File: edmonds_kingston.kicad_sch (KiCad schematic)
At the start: 22 parts

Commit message: single ferry track checkpoint
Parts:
- removed LED1015, LED1016, LED1017, LED1018, LED1019, LED1020, LED1021, LED1022, LED1023, LED1024: WS2812B-2020, EasyEDA:LED-SMD_4P-L2.0-W2.0-TL_WS2812B-2020, symbol EasyEDA:WS2812B-2020

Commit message: checkpoint before label plugin
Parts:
- added LED1011, LED1012, LED1013, LED1014: WS2812B-2020, EasyEDA:LED-SMD_4P-L2.0-W2.0-TL_WS2812B-2020, symbol EasyEDA:WS2812B-2020
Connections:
- net +VLED: now also LED1011.4 (VDD), LED1012.4 (VDD), LED1013.4 (VDD), LED1014.4 (VDD)
- net GND: now also LED1011.2 (GND), LED1012.2 (GND), LED1013.2 (GND), LED1014.2 (GND)
- net at LED1010.1 (DO): now also LED1011.3 (DI)
- new net: LED1013.1 (DO), LED1014.3 (DI)
- new net: LED1012.1 (DO), LED1013.3 (DI)
- new net: LED1011.1 (DO), LED1012.3 (DI)

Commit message: Add rail labels
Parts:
- renumbered LED447 to LED1001, LED1001 to LED1002, LED1002 to LED1003, LED1003 to LED1004, LED1004 to LED1005, LED1005 to LED1006, LED1006 to LED1007, LED1007 to LED1008, LED1008 to LED1009, LED1009 to LED1010, LED1010 to LED1011, LED1011 to LED1012, LED1012 to LED1013, LED1013 to LED1014, LED1014 to LED1015
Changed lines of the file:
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@@
 		(dnp no)
 		(fields_autoplaced yes)
-		(property "Reference" "LED1003"
+		(property "Reference" "LED1004"
 			(at 93.98 26.67 0)
 			(show_name no)
@@
 			(project "transit"
 				(path "/3763eade-a8c8-4ec0-9cf2-9db4442b4ee5/153adc6e-a3b0-4527-a19a-87e28aab4b4d/8f5c64ad-8b76-4e92-82ed-624af7bc34b2"
-					(reference "LED1003")
+					(reference "LED1004")
 					(unit 1)
 				)
@@
 		(dnp no)
 		(fields_autoplaced yes)
-		(property "Reference" "LED1013"
+		(property "Reference" "LED1014"
 			(at 185.42 46.99 0)
 			(show_name no)
@@
 			(project "transit"
 				(path "/3763eade-a8c8-4ec0-9cf2-9db4442b4ee5/153adc6e-a3b0-4527-a19a-87e28aab4b4d/8f5c64ad-8b76-4e92-82ed-624af7bc34b2"
-					(reference "LED1013")
+					(reference "LED1014")
 					(unit 1)
 				)
@@
 		(dnp no)
 		(fields_autoplaced yes)
-		(property "Reference" "LED1014"
+		(property "Reference" "LED1015"
 			(at 207.01 46.99 0)
 			(show_name no)
@@
 			(project "transit"
 				(path "/3763eade-a8c8-4ec0-9cf2-9db4442b4ee5/153adc6e-a3b0-4527-a19a-87e28aab4b4d/8f5c64ad-8b76-4e92-82ed-624af7bc34b2"
-					(reference "LED1014")
+					(reference "LED1015")
 					(unit 1)
 				)
@@
 		(dnp no)
 		(fields_autoplaced yes)
-		(property "Reference" "LED1008"
+		(property "Reference" "LED1009"
 			(at 83.82 46.99 0)
 			(show_name no)
@@
 			(project "transit"
 				(path "/3763eade-a8c8-4ec0-9cf2-9db4442b4ee5/153adc6e-a3b0-4527-a19a-87e28aab4b4d/8f5c64ad-8b76-4e92-82ed-624af7bc34b2"
-					(reference "LED1008")
+					(reference "LED1009")
 					(unit 1)
 				)
@@
 		(dnp no)
 		(fields_autoplaced yes)
-		(property "Reference" "LED1012"
+		(property "Reference" "LED1013"
 			(at 165.1 46.99 0)
 			(show_name no)
@@
 			(project "transit"
 				(path "/3763eade-a8c8-4ec0-9cf2-9db4442b4ee5/153adc6e-a3b0-4527-a19a-87e28aab4b4d/8f5c64ad-8b76-4e92-82ed-624af7bc34b2"
-					(reference "LED1012")
+					(reference "LED1013")
 					(unit 1)
 				)
@@
 		(dnp no)
 		(fields_autoplaced yes)
-		(property "Reference" "LED1001"
+		(property "Reference" "LED1002"
 			(at 53.34 26.67 0)
 			(show_name no)
@@
 			(project "transit"
 				(path "/3763eade-a8c8-4ec0-9cf2-9db4442b4ee5/153adc6e-a3b0-4527-a19a-87e28aab4b4d/8f5c64ad-8b76-4e92-82ed-624af7bc34b2"
-					(reference "LED1001")
+					(reference "LED1002")
 					(unit 1)
 				)
@@
 		(dnp no)
 		(fields_autoplaced yes)
-		(property "Reference" "LED1002"
+		(property "Reference" "LED1003"
 			(at 73.66 26.67 0)
 			(show_name no)
@@
 			(project "transit"
 				(path "/3763eade-a8c8-4ec0-9cf2-9db4442b4ee5/153adc6e-a3b0-4527-a19a-87e28aab4b4d/8f5c64ad-8b76-4e92-82ed-624af7bc34b2"
-					(reference "LED1002")
+					(reference "LED1003")
 					(unit 1)
 				)
@@
 		(dnp no)
 		(fields_autoplaced yes)
-		(property "Reference" "LED1011"
+		(property "Reference" "LED1012"
 			(at 144.78 46.99 0)
 			(show_name no)
@@
 			(project "transit"
 				(path "/3763eade-a8c8-4ec0-9cf2-9db4442b4ee5/153adc6e-a3b0-4527-a19a-87e28aab4b4d/8f5c64ad-8b76-4e92-82ed-624af7bc34b2"
-					(reference "LED1011")
+					(reference "LED1012")
 					(unit 1)
 				)
@@
 		(dnp no)
 		(fields_autoplaced yes)
-		(property "Reference" "LED1005"
+		(property "Reference" "LED1006"
 			(at 134.62 26.67 0)
 			(show_name no)
@@
 			(project "transit"
 				(path "/3763eade-a8c8-4ec0-9cf2-9db4442b4ee5/153adc6e-a3b0-4527-a19a-87e28aab4b4d/8f5c64ad-8b76-4e92-82ed-624af7bc34b2"
-					(reference "LED1005")
+					(reference "LED1006")
 					(unit 1)
 				)
@@
 		(dnp no)
 		(fields_autoplaced yes)
-		(property "Reference" "LED1009"
+		(property "Reference" "LED1010"
 			(at 104.14 46.99 0)
 			(show_name no)
@@
 			(project "transit"
 				(path "/3763eade-a8c8-4ec0-9cf2-9db4442b4ee5/153adc6e-a3b0-4527-a19a-87e28aab4b4d/8f5c64ad-8b76-4e92-82ed-624af7bc34b2"
-					(reference "LED1009")
+					(reference "LED1010")
 					(unit 1)
 				)
@@
 		(dnp no)
 		(fields_autoplaced yes)
-		(property "Reference" "LED1007"
+		(property "Reference" "LED1008"
 			(at 63.5 46.99 0)
 			(show_name no)
@@
 			(project "transit"
 				(path "/3763eade-a8c8-4ec0-9cf2-9db4442b4ee5/153adc6e-a3b0-4527-a19a-87e28aab4b4d/8f5c64ad-8b76-4e92-82ed-624af7bc34b2"
-					(reference "LED1007")
+					(reference "LED1008")
 					(unit 1)
 				)
@@
 		(dnp no)
 		(fields_autoplaced yes)
-		(property "Reference" "LED1004"
+		(property "Reference" "LED1005"
 			(at 114.3 26.67 0)
 			(show_name no)
@@
 			(project "transit"
 				(path "/3763eade-a8c8-4ec0-9cf2-9db4442b4ee5/153adc6e-a3b0-4527-a19a-87e28aab4b4d/8f5c64ad-8b76-4e92-82ed-624af7bc34b2"
-					(reference "LED1004")
+					(reference "LED1005")
 					(unit 1)
 				)
@@
 		(dnp no)
 		(fields_autoplaced yes)
-		(property "Reference" "LED1010"
+		(property "Reference" "LED1011"
 			(at 124.46 46.99 0)
 			(show_name no)
@@
 			(project "transit"
 				(path "/3763eade-a8c8-4ec0-9cf2-9db4442b4ee5/153adc6e-a3b0-4527-a19a-87e28aab4b4d/8f5c64ad-8b76-4e92-82ed-624af7bc34b2"
-					(reference "LED1010")
+					(reference "LED1011")
 					(unit 1)
 				)
@@
 		(dnp no)
 		(fields_autoplaced yes)
-		(property "Reference" "LED1006"
+		(property "Reference" "LED1007"
 			(at 154.94 26.67 0)
 			(show_name no)
@@
 			(project "transit"
 				(path "/3763eade-a8c8-4ec0-9cf2-9db4442b4ee5/153adc6e-a3b0-4527-a19a-87e28aab4b4d/8f5c64ad-8b76-4e92-82ed-624af7bc34b2"
-					(reference "LED1006")
+					(reference "LED1007")
 					(unit 1)
 				)
@@
 		(in_pos_files yes)
 		(dnp no)
-		(property "Reference" "LED447"
+		(property "Reference" "LED1001"
 			(at 31.75 26.67 0)
 			(show_name no)
@@
 			(project "transit"
 				(path "/3763eade-a8c8-4ec0-9cf2-9db4442b4ee5/153adc6e-a3b0-4527-a19a-87e28aab4b4d/8f5c64ad-8b76-4e92-82ed-624af7bc34b2"
-					(reference "LED447")
+					(reference "LED1001")
 					(unit 1)
 				)

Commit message: routing complete
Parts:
- removed C402: 150u, EasyEDA:CAP-SMD_L3.5-W2.8, symbol EasyEDA:CL21B106KOQNNNE
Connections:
- net +VLED: now also LED1003.4 (VDD)
- net at LED1004.1 (DO): now also LED1003.3 (DI); no longer LED1005.3 (DI)
- net at LED1003.1 (DO): now also LED1002.3 (DI); no longer LED1004.3 (DI)
- net at LED1014.1 (DO): now also LED1013.3 (DI); no longer LED1015.3 (DI)
- net at LED1013.1 (DO): now also LED1012.3 (DI); no longer LED1014.3 (DI)
- net at LED1015.1 (DO): now also LED1014.3 (DI)
- net at LED1010.3 (DI): now also LED1011.1 (DO); no longer LED1009.1 (DO)
- net at LED1009.3 (DI): now also LED1010.1 (DO); no longer LED1008.1 (DO)
- net at LED1012.1 (DO): now also LED1011.3 (DI); no longer LED1013.3 (DI)
- net at LED1002.1 (DO): now also LED1001.4 (DIN); no longer LED1003.3 (DI)
- net EDMONDS_MUKILTEO: now reaches LED1001.2 (DOUT)
- net EDMONDS_MUKILTEO: no longer LED1002.3 (DI)
- net at LED1007.3 (DI): now also LED1008.1 (DO); no longer LED1006.1 (DO)
- net at LED1005.1 (DO): now also LED1004.3 (DI); no longer LED1006.3 (DI)
- net at LED1008.3 (DI): now also LED1009.1 (DO); no longer LED1007.1 (DO)
- new net: LED1005.3 (DI), LED1006.1 (DO)
- new net: LED1006.3 (DI), LED1007.1 (DO)
- new net KINGSTON_EDMONDS: LED1015.3 (DI)
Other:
- moved on the sheet: LED1001

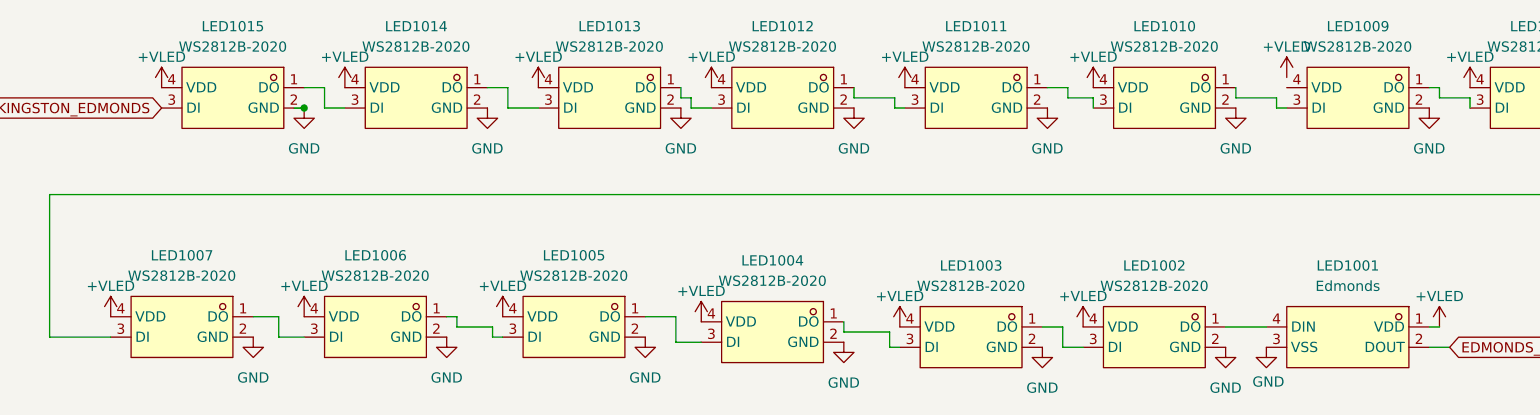
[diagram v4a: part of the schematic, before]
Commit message: reflow reference designators
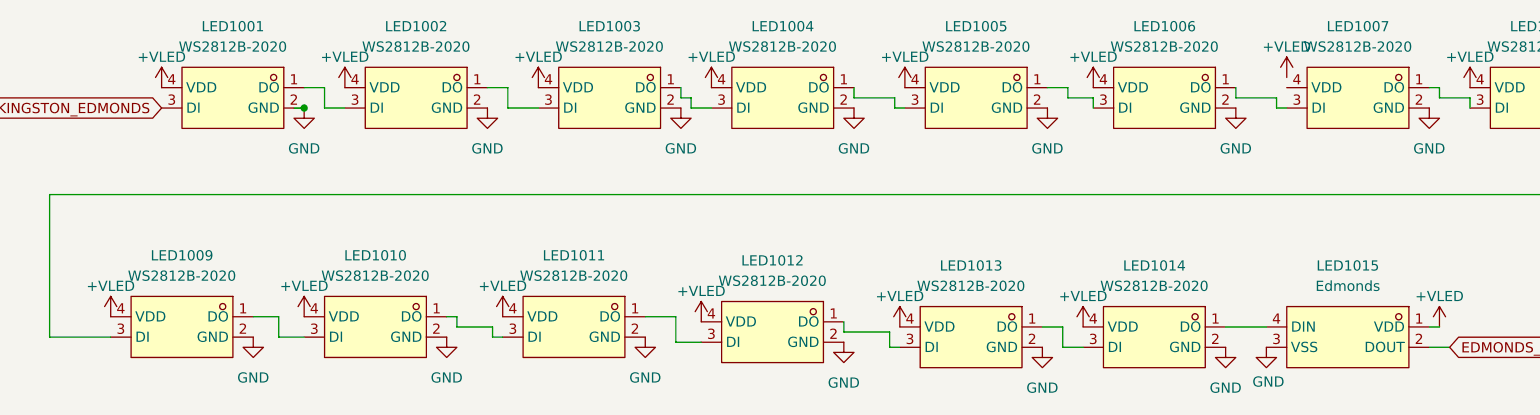
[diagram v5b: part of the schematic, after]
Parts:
- renumbered LED1015 to LED1001, LED1014 to LED1002, LED1013 to LED1003, LED1012 to LED1004, LED1011 to LED1005, LED1010 to LED1006, LED1009 to LED1007, LED1007 to LED1009, LED1006 to LED1010, LED1005 to LED1011, LED1004 to LED1012, LED1003 to LED1013, LED1002 to LED1014, LED1001 to LED1015
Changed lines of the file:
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@@
 		(dnp no)
 		(fields_autoplaced yes)
-		(property "Reference" "LED1002"
+		(property "Reference" "LED1014"
 			(at 171.45 64.135 0)
 			(show_name no)
@@
 			(project "transit"
 				(path "/3763eade-a8c8-4ec0-9cf2-9db4442b4ee5/153adc6e-a3b0-4527-a19a-87e28aab4b4d/8f5c64ad-8b76-4e92-82ed-624af7bc34b2"
-					(reference "LED1002")
+					(reference "LED1014")
 					(unit 1)
 				)
@@
 		(dnp no)
 		(fields_autoplaced yes)
-		(property "Reference" "LED1010"
+		(property "Reference" "LED1006"
 			(at 172.72 34.29 0)
 			(show_name no)
@@
 			(project "transit"
 				(path "/3763eade-a8c8-4ec0-9cf2-9db4442b4ee5/153adc6e-a3b0-4527-a19a-87e28aab4b4d/8f5c64ad-8b76-4e92-82ed-624af7bc34b2"
-					(reference "LED1010")
+					(reference "LED1006")
 					(unit 1)
 				)
@@
 		(dnp no)
 		(fields_autoplaced yes)
-		(property "Reference" "LED1011"
+		(property "Reference" "LED1005"
 			(at 149.225 34.29 0)
 			(show_name no)
@@
 			(project "transit"
 				(path "/3763eade-a8c8-4ec0-9cf2-9db4442b4ee5/153adc6e-a3b0-4527-a19a-87e28aab4b4d/8f5c64ad-8b76-4e92-82ed-624af7bc34b2"
-					(reference "LED1011")
+					(reference "LED1005")
 					(unit 1)
 				)
@@
 		(dnp no)
 		(fields_autoplaced yes)
-		(property "Reference" "LED1013"
+		(property "Reference" "LED1003"
 			(at 103.505 34.29 0)
 			(show_name no)
@@
 			(project "transit"
 				(path "/3763eade-a8c8-4ec0-9cf2-9db4442b4ee5/153adc6e-a3b0-4527-a19a-87e28aab4b4d/8f5c64ad-8b76-4e92-82ed-624af7bc34b2"
-					(reference "LED1013")
+					(reference "LED1003")
 					(unit 1)
 				)
@@
 		(dnp no)
 		(fields_autoplaced yes)
-		(property "Reference" "LED1009"
+		(property "Reference" "LED1007"
 			(at 196.85 34.29 0)
 			(show_name no)
@@
 			(project "transit"
 				(path "/3763eade-a8c8-4ec0-9cf2-9db4442b4ee5/153adc6e-a3b0-4527-a19a-87e28aab4b4d/8f5c64ad-8b76-4e92-82ed-624af7bc34b2"
-					(reference "LED1009")
+					(reference "LED1007")
 					(unit 1)
 				)
@@
 		(dnp no)
 		(fields_autoplaced yes)
-		(property "Reference" "LED1015"
+		(property "Reference" "LED1001"
 			(at 56.515 34.29 0)
 			(show_name no)
@@
 			(project "transit"
 				(path "/3763eade-a8c8-4ec0-9cf2-9db4442b4ee5/153adc6e-a3b0-4527-a19a-87e28aab4b4d/8f5c64ad-8b76-4e92-82ed-624af7bc34b2"
-					(reference "LED1015")
+					(reference "LED1001")
 					(unit 1)
 				)
@@
 		(dnp no)
 		(fields_autoplaced yes)
-		(property "Reference" "LED1012"
+		(property "Reference" "LED1004"
 			(at 125.095 34.29 0)
 			(show_name no)
@@
 			(project "transit"
 				(path "/3763eade-a8c8-4ec0-9cf2-9db4442b4ee5/153adc6e-a3b0-4527-a19a-87e28aab4b4d/8f5c64ad-8b76-4e92-82ed-624af7bc34b2"
-					(reference "LED1012")
+					(reference "LED1004")
 					(unit 1)
 				)
@@
 		(dnp no)
 		(fields_autoplaced yes)
-		(property "Reference" "LED1003"
+		(property "Reference" "LED1013"
 			(at 148.59 64.135 0)
 			(show_name no)
@@
 			(project "transit"
 				(path "/3763eade-a8c8-4ec0-9cf2-9db4442b4ee5/153adc6e-a3b0-4527-a19a-87e28aab4b4d/8f5c64ad-8b76-4e92-82ed-624af7bc34b2"
-					(reference "LED1003")
+					(reference "LED1013")
 					(unit 1)
 				)
@@
 		(dnp no)
 		(fields_autoplaced yes)
-		(property "Reference" "LED1014"
+		(property "Reference" "LED1002"
 			(at 79.375 34.29 0)
 			(show_name no)
@@
 			(project "transit"
 				(path "/3763eade-a8c8-4ec0-9cf2-9db4442b4ee5/153adc6e-a3b0-4527-a19a-87e28aab4b4d/8f5c64ad-8b76-4e92-82ed-624af7bc34b2"
-					(reference "LED1014")
+					(reference "LED1002")
 					(unit 1)
 				)
@@
 		(dnp no)
 		(fields_autoplaced yes)
-		(property "Reference" "LED1005"
+		(property "Reference" "LED1011"
 			(at 99.06 62.865 0)
 			(show_name no)
@@
 			(project "transit"
 				(path "/3763eade-a8c8-4ec0-9cf2-9db4442b4ee5/153adc6e-a3b0-4527-a19a-87e28aab4b4d/8f5c64ad-8b76-4e92-82ed-624af7bc34b2"
-					(reference "LED1005")
+					(reference "LED1011")
 					(unit 1)
 				)
@@
 		(dnp no)
 		(fields_autoplaced yes)
-		(property "Reference" "LED1006"
+		(property "Reference" "LED1010"
 			(at 74.295 62.865 0)
 			(show_name no)
@@
 			(project "transit"
 				(path "/3763eade-a8c8-4ec0-9cf2-9db4442b4ee5/153adc6e-a3b0-4527-a19a-87e28aab4b4d/8f5c64ad-8b76-4e92-82ed-624af7bc34b2"
-					(reference "LED1006")
+					(reference "LED1010")
 					(unit 1)
 				)
@@
 		(dnp no)
 		(fields_autoplaced yes)
-		(property "Reference" "LED1007"
+		(property "Reference" "LED1009"
 			(at 50.165 62.865 0)
 			(show_name no)
@@
 			(project "transit"
 				(path "/3763eade-a8c8-4ec0-9cf2-9db4442b4ee5/153adc6e-a3b0-4527-a19a-87e28aab4b4d/8f5c64ad-8b76-4e92-82ed-624af7bc34b2"
-					(reference "LED1007")
+					(reference "LED1009")
 					(unit 1)
 				)
@@
 		(dnp no)
 		(fields_autoplaced yes)
-		(property "Reference" "LED1004"
+		(property "Reference" "LED1012"
 			(at 123.825 63.5 0)
 			(show_name no)
@@
 			(project "transit"
 				(path "/3763eade-a8c8-4ec0-9cf2-9db4442b4ee5/153adc6e-a3b0-4527-a19a-87e28aab4b4d/8f5c64ad-8b76-4e92-82ed-624af7bc34b2"
-					(reference "LED1004")
+					(reference "LED1012")
 					(unit 1)
 				)
@@
 		(in_pos_files yes)
 		(dnp no)
-		(property "Reference" "LED1001"
+		(property "Reference" "LED1015"
 			(at 195.58 64.135 0)
 			(show_name no)
@@
 			(project "transit"
 				(path "/3763eade-a8c8-4ec0-9cf2-9db4442b4ee5/153adc6e-a3b0-4527-a19a-87e28aab4b4d/8f5c64ad-8b76-4e92-82ed-624af7bc34b2"
-					(reference "LED1001")
+					(reference "LED1015")
 					(unit 1)
 				)
